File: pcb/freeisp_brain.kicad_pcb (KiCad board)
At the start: 2 copper layers, 115 x 115 mm, 33 parts, among them J1 12V IN, J10 BUZZER, J11 HORN, J13 BOOST IN+ IN- OUT+ OUT-, J4 TFT, J5 RC522, J7 REED, J8 LED R, J9 LED G, K1 HORN RLY, U1 BUCK IN+ IN- OUT+ OUT-, U2 CHARGER IN+ IN- OUT+ OUT-, U3A ESP32 L, U3B ESP32 R, U4 MPU-6050

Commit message: Print calibration on the fit-check sheet: ruler + the two key dimensions
Francis's paper test had ~6 pins landing then the rest drifting off, and he
measured the printed outline at 9.56cm where the board was 10.00cm - his
printer shrank the page to 95.6%. Over the 45.72mm pin row that is 2.0mm of
accumulated error, which is exactly the symptom.

Verified the design is not at fault: every pad gap on all five connectors is
exactly 2.54000mm, ESP32 pin1->pin19 spans 45.7200mm, rows are 25.4000mm
apart, outline is 115.000mm square.

Added to the fit-check plot, on Dwgs.User so the fab never makes it:
- a 100mm ruler with 10mm ticks, labelled "MEASURE THIS LINE FIRST"
- the ESP32's two critical dimensions called out (45.72mm pin span,
  25.40mm row-to-row) so a scaled print is caught on the sheet itself

fitcheck_1to1.pdf now exports with Dwgs.User included. Gerber export must
NOT include that layer.

Co-Authored-By: Claude Opus 5 (1M context) <noreply@anthropic.com>
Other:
- board text added: "0"
- board text added: "100"
- board text added: "100.00 mm - MEASURE THIS LINE FIRST"
- board text added: "25.40 mm row to row"
- board text added: "45.72 mm pin 1 to pin 19"
- board text added: "50"
- board text added: "not exactly 100 mm? the printer scaled the page - reprint at 100% / Actual Size, scaling OFF"
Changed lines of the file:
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@@
 		(15 "B.Paste" user)
 		(17 "Dwgs.User" user "User.Drawings")
+		(45 "User.1" user)
 		(19 "Cmts.User" user "User.Comments")
 		(21 "Eco1.User" user "User.Eco1")
@@
 			)
 		)
+	)
+	(gr_line
+		(start 67.5000 164.0000)
+		(end 167.5000 164.0000)
+		(stroke
+			(width 0.35)
+			(type default)
+		)
+		(layer "Dwgs.User")
+	)
+	(gr_line
+		(start 67.5000 164.0000)
+		(end 67.5000 160.8000)
+		(stroke
+			(width 0.3)
+			(type default)
+		)
+		(layer "Dwgs.User")
+	)
+	(gr_text "0"
+		(at 67.5000 158.4000)
+		(layer "Dwgs.User")
+		(effects
+			(font
+				(size 2.2 2.2)
+				(thickness 0.25)
+			)
+		)
+	)
+	(gr_line
+		(start 77.5000 164.0000)
+		(end 77.5000 162.2000)
+		(stroke
+			(width 0.3)
+			(type default)
+		)
+		(layer "Dwgs.User")
+	)
+	(gr_line
+		(start 87.5000 164.0000)
+		(end 87.5000 162.2000)
+		(stroke
+			(width 0.3)
+			(type default)
+		)
+		(layer "Dwgs.User")
+	)
+	(gr_line
+		(start 97.5000 164.0000)
+		(end 97.5000 162.2000)
+		(stroke
+			(width 0.3)
+			(type default)
+		)
+		(layer "Dwgs.User")
+	)
+	(gr_line
+		(start 107.5000 164.0000)
+		(end 107.5000 162.2000)
+		(stroke
+			(width 0.3)
+			(type default)
+		)
+		(layer "Dwgs.User")
+	)
+	(gr_line
+		(start 117.5000 164.0000)
+		(end 117.5000 160.8000)
+		(stroke
+			(width 0.3)
+			(type default)
+		)
+		(layer "Dwgs.User")
+	)
+	(gr_text "50"
+		(at 117.5000 158.4000)
+		(layer "Dwgs.User")
+		(effects
+			(font
+				(size 2.2 2.2)
+				(thickness 0.25)
+			)
+		)
+	)
+	(gr_line
+		(start 127.5000 164.0000)
+		(end 127.5000 162.2000)
+		(stroke
+			(width 0.3)
+			(type default)
+		)
+		(layer "Dwgs.User")
+	)
+	(gr_line
+		(start 137.5000 164.0000)
+		(end 137.5000 162.2000)
+		(stroke
+			(width 0.3)
+			(type default)
+		)
+		(layer "Dwgs.User")
+	)
+	(gr_line
+		(start 147.5000 164.0000)
+		(end 147.5000 162.2000)
+		(stroke
+			(width 0.3)
+			(type default)
+		)
+		(layer "Dwgs.User")
+	)
+	(gr_line
+		(start 157.5000 164.0000)
+		(end 157.5000 162.2000)
+		(stroke
+			(width 0.3)
+			(type default)
+		)
+		(layer "Dwgs.User")
+	)
+	(gr_line
+		(start 167.5000 164.0000)
+		(end 167.5000 160.8000)
+		(stroke
+			(width 0.3)
+			(type default)
+		)
+		(layer "Dwgs.User")
+	)
+	(gr_text "100"
+		(at 167.5000 158.4000)
+		(layer "Dwgs.User")
+		(effects
+			(font
+				(size 2.2 2.2)
+				(thickness 0.25)
+			)
+		)
+	)
+	(gr_text "100.00 mm  -  MEASURE THIS LINE FIRST"
+		(at 117.5000 169.0000)
+		(layer "Dwgs.User")
+		(effects
+			(font
+				(size 2.6 2.6)
+				(thickness 0.25)
+			)
+		)
+	)
+	(gr_text "not exactly 100 mm? the printer scaled the page - reprint at 100% / Actual Size, scaling OFF"
+		(at 117.5000 173.4000)
+		(layer "Dwgs.User")
+		(effects
+			(font
+				(size 1.9 1.9)
+				(thickness 0.25)
+			)
+		)
+	)
+	(gr_line
+		(start 86.0000 74.0000)
+		(end 86.0000 119.7200)
+		(stroke
+			(width 0.3)
+			(type default)
+		)
+		(layer "Dwgs.User")
+	)
+	(gr_line
+		(start 84.6000 74.0000)
+		(end 87.4000 74.0000)
+		(stroke
+			(width 0.3)
+			(type default)
+		)
+		(layer "Dwgs.User")
+	)
+	(gr_line
+		(start 84.6000 119.7200)
+		(end 87.4000 119.7200)
+		(stroke
+			(width 0.3)
+			(type default)
+		)
+		(layer "Dwgs.User")
+	)
+	(gr_text "45.72 mm  pin 1 to pin 19"
+		(at 83.4000 96.9000 90)
+		(layer "Dwgs.User")
+		(effects
+			(font
+				(size 2.0 2.0)
+				(thickness 0.25)
+			)
+		)
+	)
+	(gr_line
+		(start 104.0000 64.5000)
+		(end 129.4000 64.5000)
+		(stroke
+			(width 0.3)
+			(type default)
+		)
+		(layer "Dwgs.User")
+	)
+	(gr_line
+		(start 104.0000 63.1000)
+		(end 104.0000 65.9000)
+		(stroke
+			(width 0.3)
+			(type default)
+		)
+		(layer "Dwgs.User")
+	)
+	(gr_line
+		(start 129.4000 63.1000)
+		(end 129.4000 65.9000)
+		(stroke
+			(width 0.3)
+			(type default)
+		)
+		(layer "Dwgs.User")
+	)
+	(gr_text "25.40 mm  row to row"
+		(at 116.7000 62.2000)
+		(layer "Dwgs.User")
+		(effects
+			(font
+				(size 2.0 2.0)
+				(thickness 0.25)
+			)
+		)

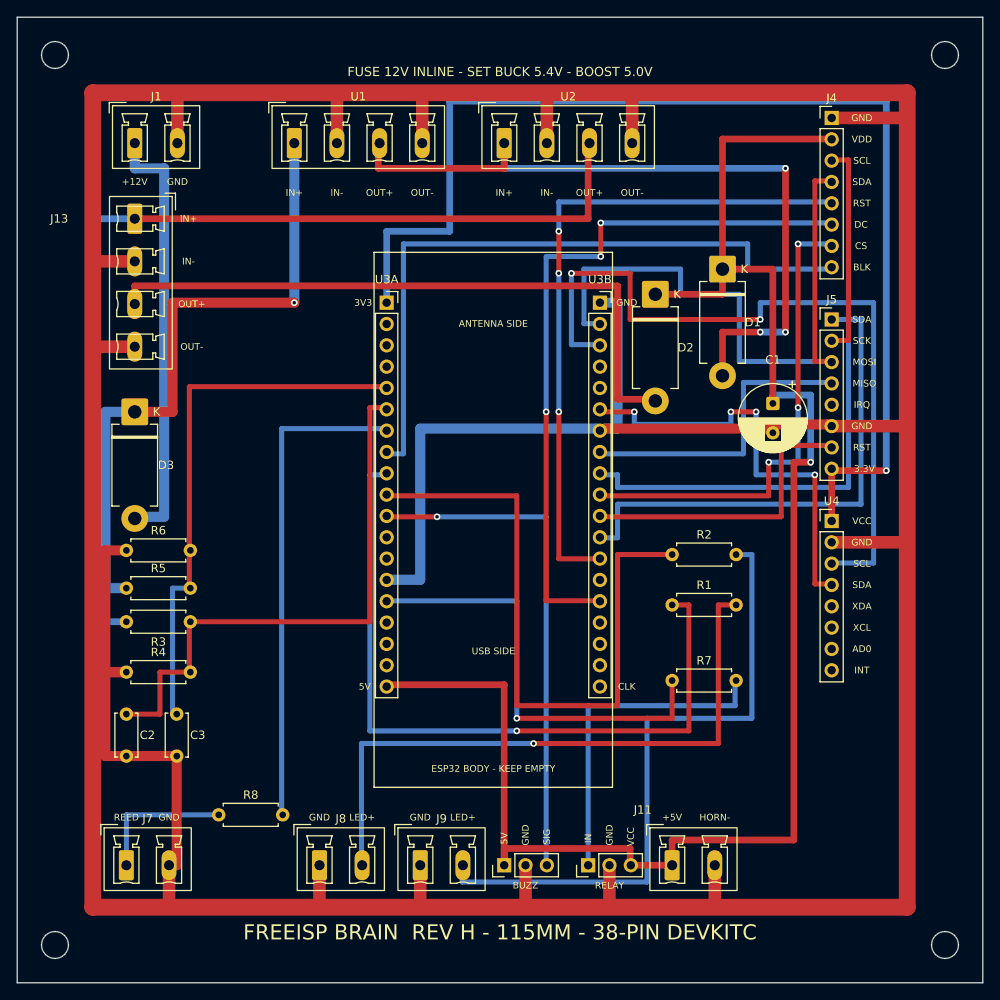
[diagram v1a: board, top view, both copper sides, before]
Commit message: J14 expansion header: every spare pin brought out for later
Francis's call, and a good one - cheap now, impossible after the boards are
made: "we can always have extra pins, something can come up... for example
we can decide to add buttons, you never know, so we can always reprogram
later and have a provision."

2x5 header beside the ESP32 carrying 3V3, 5V_SYS, three GNDs and the five
usable spare pins: D36 and D39 (input-only, ADC1), D14 (full GPIO with an
internal pull-up - the right pin for a button), D12 (works, but a strapping
pin) and EN (reset button to ground).

TX0/RX0 stay off it deliberately - they are the USB serial port, and loading
them breaks programming and the serial monitor. The six flash pins remain
untouched and verified unconnected.

Placed beside U3A because every spare is on that column; the first attempt
sat it bottom-right and five nets had to cross the whole board, which the
router could not finish. Retry rounds raised 4 -> 7 for the denser board.

Cost: 249 -> 321 track segments, 25 -> 44 vias, 143 -> 172 plated holes.
All three checks still green: audit PASS, trace PASS (35 nets, 113
connections, 15 no-connects), DRC 0 errors 0 unconnected. Gerbers regenerated.

Co-Authored-By: Claude Opus 5 (1M context) <noreply@anthropic.com>
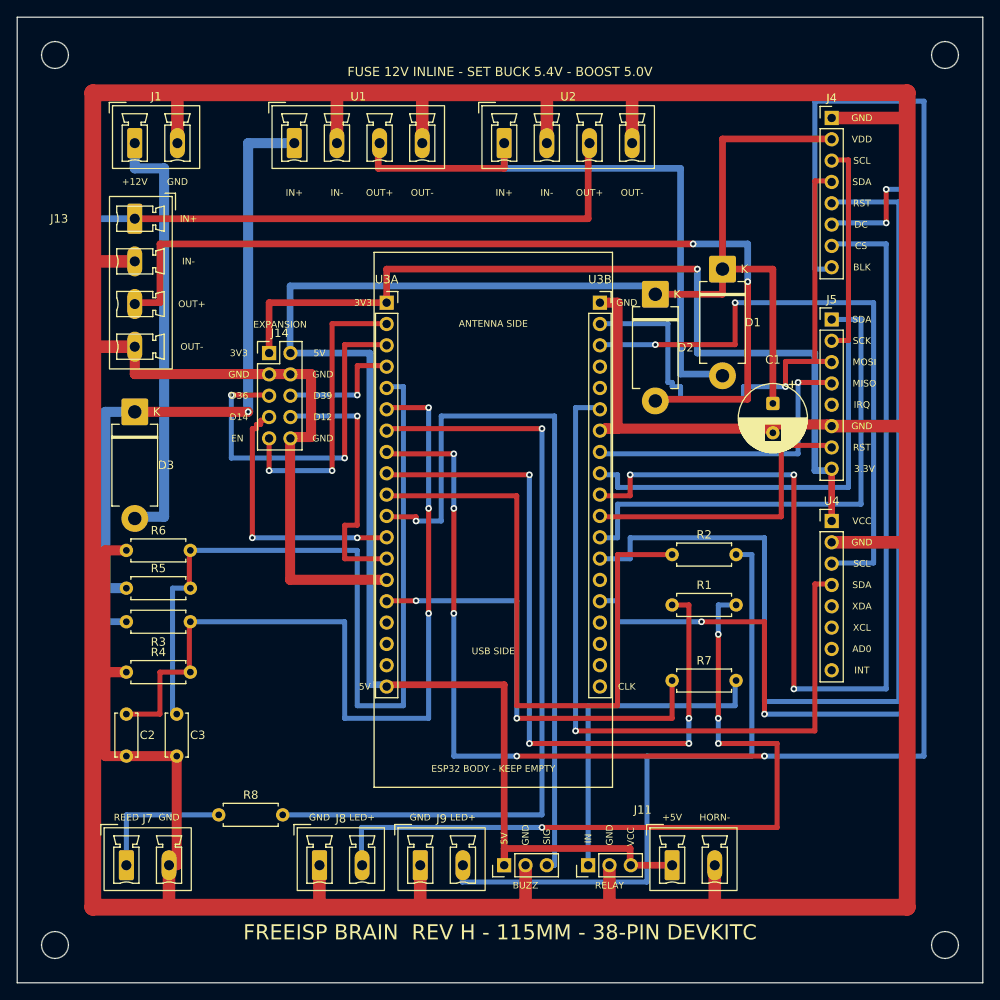
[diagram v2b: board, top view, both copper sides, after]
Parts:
- added J14: EXPANSION, Connector_PinHeader_2.54mm:PinHeader_2x05_P2.54mm_Vertical, F.Cu at (90.0, 80.0)
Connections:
- U3A pad 12: (no net) -> EXP_D14
- U3A pad 13: (no net) -> EXP_D12
- U3A pad 2: (no net) -> EXP_EN
- U3A pad 3: (no net) -> EXP_D36
- U3A pad 4: (no net) -> EXP_D39
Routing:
- net TFT_BLK: track 81.1 -> 213.1 mm, vias 0 -> 5
- net TFT_CS: track 57.7 -> 121.7 mm
- net TFT_RST: track 79.9 -> 125.1 mm, vias 3 -> 0
- net EXP_D36: track 0.00 -> 44.0 mm, vias 0 -> 2
- net TFT_DC: track 85.4 -> 126.6 mm, vias 3 -> 4
- net SENSE_MAINS: track 65.2 -> 106.1 mm
- net SDA: track 51.3 -> 89.5 mm, vias 4 -> 1
- net REED: track 58.6 -> 95.4 mm, vias 0 -> 1
- net EXP_EN: track 0.00 -> 35.3 mm, vias 0 -> 2
- net +3V3: track 140.3 -> 107.3 mm
- net SENSE_BATT: track 67.6 -> 100.6 mm, vias 0 -> 3
- net EXP_D14: track 0.00 -> 32.4 mm, vias 0 -> 2
- net +5V_BAT: track 77.7 -> 109.6 mm, vias 0 -> 2
- net EXP_D12: track 0.00 -> 31.5 mm, vias 0 -> 1
- net BUZZ: track 60.5 -> 87.4 mm
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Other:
- board text added: "D12"
- board text added: "D14"
- board text added: "D36"
- board text added: "D39"
- board text added: "EN"
- board text added: "EXPANSION"

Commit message: PCB: clear the USB cable path below the soldered-in ESP32
J10 buzzer and K1 relay headers move up beside R8/R7, J9 slides
right into K1's old spot (its body sat under the plug overmold),
J11 nudges 2mm right. Stubs + silk follow. DRC clean, audit pass,
gerbers + renders + BOM/CPL regenerated.

Co-Authored-By: Claude Fable 5 <noreply@anthropic.com>
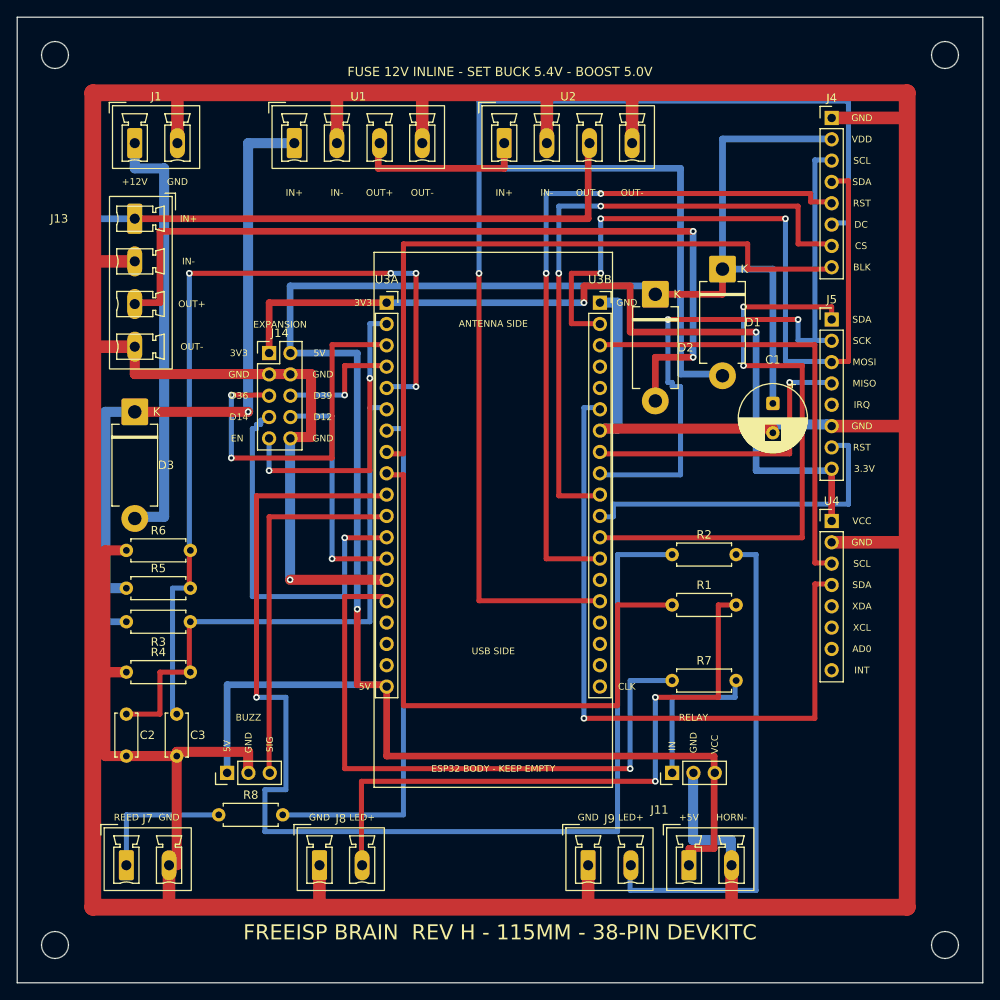
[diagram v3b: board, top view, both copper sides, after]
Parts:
- moved J10 34.8 mm to (85.0, 130.0)
- moved J9 20.0 mm to (128.0, 141.0)
- moved K1 14.9 mm to (138.0, 130.0)
- moved J11 2.00 mm to (140.0, 141.0)
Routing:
- net TFT_BLK: track 213.1 -> 81.1 mm, vias 5 -> 0
- net LED_G: track 77.0 -> 143.0 mm, vias 0 -> 1
- net TFT_CS: track 121.7 -> 76.5 mm, vias 3 -> 2
- net BUZZ: track 87.4 -> 44.5 mm, vias 1 -> 0
- net TFT_RST: track 125.1 -> 84.9 mm, vias 0 -> 2
- net +5V_SYS: track 224.5 -> 257.8 mm, vias 0 -> 1
- net SENSE_BATT: track 100.6 -> 67.6 mm, vias 3 -> 0
- net REED: track 95.4 -> 62.4 mm, vias 1 -> 0
- net HORN_IN: track 52.5 -> 75.6 mm, vias 2 -> 1
- net MOSI: track 66.6 -> 89.4 mm, vias 1 -> 3
- net HORN_DRV: track 39.5 -> 18.5 mm
- net SCL: track 73.6 -> 53.6 mm, vias 2 -> 0
- net GND: track 650.4 -> 667.5 mm, vias 0 -> 1
- net LED_G_A: track 77.4 -> 60.4 mm
- net LED_R_A: track 89.6 -> 75.6 mm, vias 4 -> 2
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
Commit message: Relay header silk reads S + - , the words on Francis's actual relay
His Tongling JQC-3FF-S-Z prints S + - . The board printed IN GND VCC,
so matching the module meant translating in your head at the bench --
exactly what the silk exists to avoid. The pins and nets are unchanged;
only the three words moved to the ones on the part in hand.

Gerbers re-exported. DRC still 0 errors, 0 unconnected.

Co-Authored-By: Claude Opus 5 (1M context) <noreply@anthropic.com>
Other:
- board text added: "+"
- board text added: "-"
- board text added: "S"
- board text removed: "IN"
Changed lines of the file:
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@@
 		)
 	)
-	(gr_text "IN"
+	(gr_text "S"
 		(at 138.0000 126.8000 90)
 		(layer "F.SilkS")
@@
 		)
 	)
-	(gr_text "GND"
+	(gr_text "-"
 		(at 140.5400 126.4000 90)
 		(layer "F.SilkS")
@@
 		)
 	)
-	(gr_text "VCC"
+	(gr_text "+"
 		(at 143.0800 126.6000 90)
 		(layer "F.SilkS")
